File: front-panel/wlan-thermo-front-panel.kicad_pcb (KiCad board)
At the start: 2 copper layers, 54.7 x 43.5 mm, 26 parts, among them IC1 ME6211C33M5G-N, J1 PROG_HDR, J2 Conn_01x02, J3 Conn_01x02, Q1 UMH3N, SW1 SW_Push, SW2 RotaryEncoder_Switch, U1 ESP-12F, U2 SHT4x, U3 SSD1306

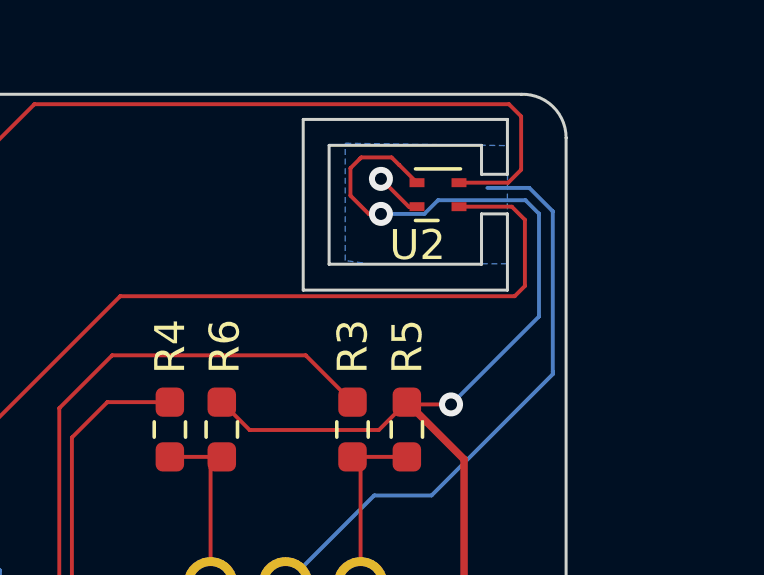
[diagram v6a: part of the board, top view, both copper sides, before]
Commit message: Removed (exposed) ground plane from sensor area (rev 1.2)
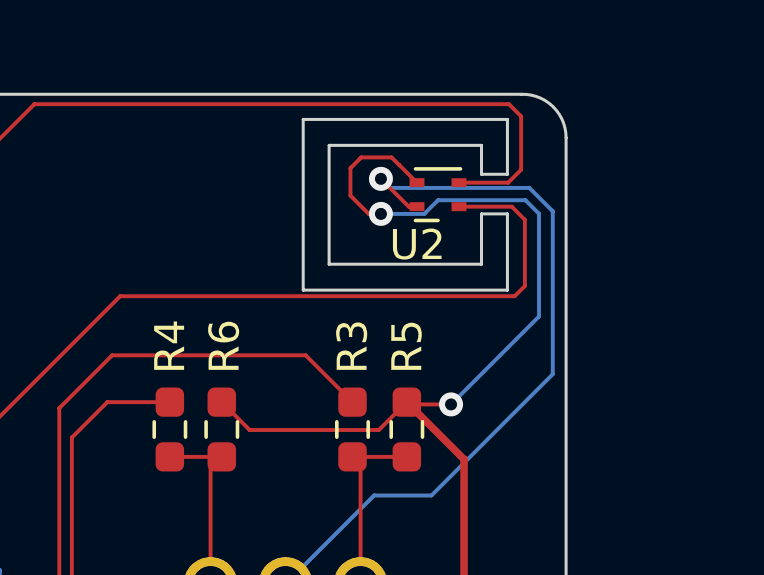
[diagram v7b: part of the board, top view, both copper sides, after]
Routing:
- net GND: track 47.9 -> 51.6 mm
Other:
- board text added: "WLAN Thermostat Frontpanel v1.2 (2023)"
- board text removed: "WLAN Thermostat Frontpanel v1.1 (2023)"
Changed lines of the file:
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@@
       (stroke (width 0) (type solid)) (fill solid) (layer "B.SilkS"))
   )
-  (gr_rect (start 146.5658 40.8806) (end 149.145 42.0116)
-    (stroke (width 0.15) (type solid)) (fill solid) (layer "B.Mask"))
-  (gr_rect (start 146.5742 38.2016) (end 149.1258 39.534)
-    (stroke (width 0.15) (type solid)) (fill solid) (layer "B.Mask"))
   (gr_line locked (start 82.0655 58.4313) (end 163.5995 58.4313)
     (stroke (width 0.15) (type default)) (layer "Dwgs.User"))
@@
     (effects (font (size 1 1) (thickness 0.15)) (justify left bottom mirror))
   )
-  (gr_text "WLAN Thermostat Frontpanel\nv1.1 (2023)" (at 151.81 46.1) (layer "B.SilkS")
+  (gr_text "WLAN Thermostat Frontpanel\nv1.2 (2023)" (at 151.81 46.1) (layer "B.SilkS")
     (effects (font (size 1 1) (thickness 0.15)) (justify left bottom mirror))
   )
@@
   (via (at 103.68 68.8) (size 0.8) (drill 0.4) (layers "F.Cu" "B.Cu") (net 4))
   (via (at 110.12 62.96) (size 0.8) (drill 0.4) (layers "F.Cu" "B.Cu") (free) (net 4))
-  (segment (start 150.767802 39.57) (end 149.37 39.57) (width 0.13) (layer "B.Cu") (net 4))
-  (segment (start 151.55 45.68) (end 151.55 40.352198) (width 0.13) (layer "B.Cu") (net 4))
+  (segment (start 147.51 49.82) (end 151.55 45.78) (width 0.13) (layer "B.Cu") (net 4))
+  (segment (start 146.123001 39.57) (end 145.821401 39.2684) (width 0.13) (layer "B.Cu") (net 4))
+  (segment (start 151.55 45.78) (end 151.55 40.352198) (width 0.13) (layer "B.Cu") (net 4))
   (segment (start 142.642801 52.7755) (end 145.598301 49.82) (width 0.13) (layer "B.Cu") (net 4))
-  (segment (start 151.55 45.78) (end 151.55 45.68) (width 0.13) (layer "B.Cu") (net 4))
-  (segment (start 147.51 49.82) (end 151.55 45.78) (width 0.13) (layer "B.Cu") (net 4))
+  (segment (start 150.767802 39.57) (end 146.123001 39.57) (width 0.13) (layer "B.Cu") (net 4))
+  (segment (start 145.598301 49.82) (end 147.51 49.82) (width 0.13) (layer "B.Cu") (net 4))
   (segment (start 103.69 75.7204) (end 103.7004 75.71) (width 0.25) (layer "B.Cu") (net 4))
-  (segment (start 145.598301 49.82) (end 147.51 49.82) (width 0.13) (layer "B.Cu") (net 4))
+  (segment (start 151.55 40.352198) (end 150.767802 39.57) (width 0.13) (layer "B.Cu") (net 4))
   (segment (start 103.7004 75.71) (end 113.24 75.71) (width 0.25) (layer "B.Cu") (net 4))
-  (segment (start 151.55 40.352198) (end 150.767802 39.57) (width 0.13) (layer "B.Cu") (net 4))
   (segment (start 113.24 75.71) (end 114.88 74.07) (width 0.25) (layer "B.Cu") (net 4))
   (segment (start 146.431001 38.8028) (end 146.426401 38.8028) (width 0.13) (layer "F.Cu") (net 6))
@@
       )
     )
-  )
-  (zone (net 4) (net_name "GND") (layer "B.Cu") (hatch edge 0.5)
-    (priority 2)
-    (connect_pads yes (clearance 0.25))
-    (min_thickness 0.25) (filled_areas_thickness no)
-    (fill yes (thermal_gap 0) (thermal_bridge_width 0.5))
-    (polygon
-      (pts
-        (xy 144.632 38.0808)
-        (xy 150.0466 38.1608)
-        (xy 150.0212 42.0978)
-        (xy 145.542 42.1132)
-        (xy 144.632 41.9924)
-      )
-    )

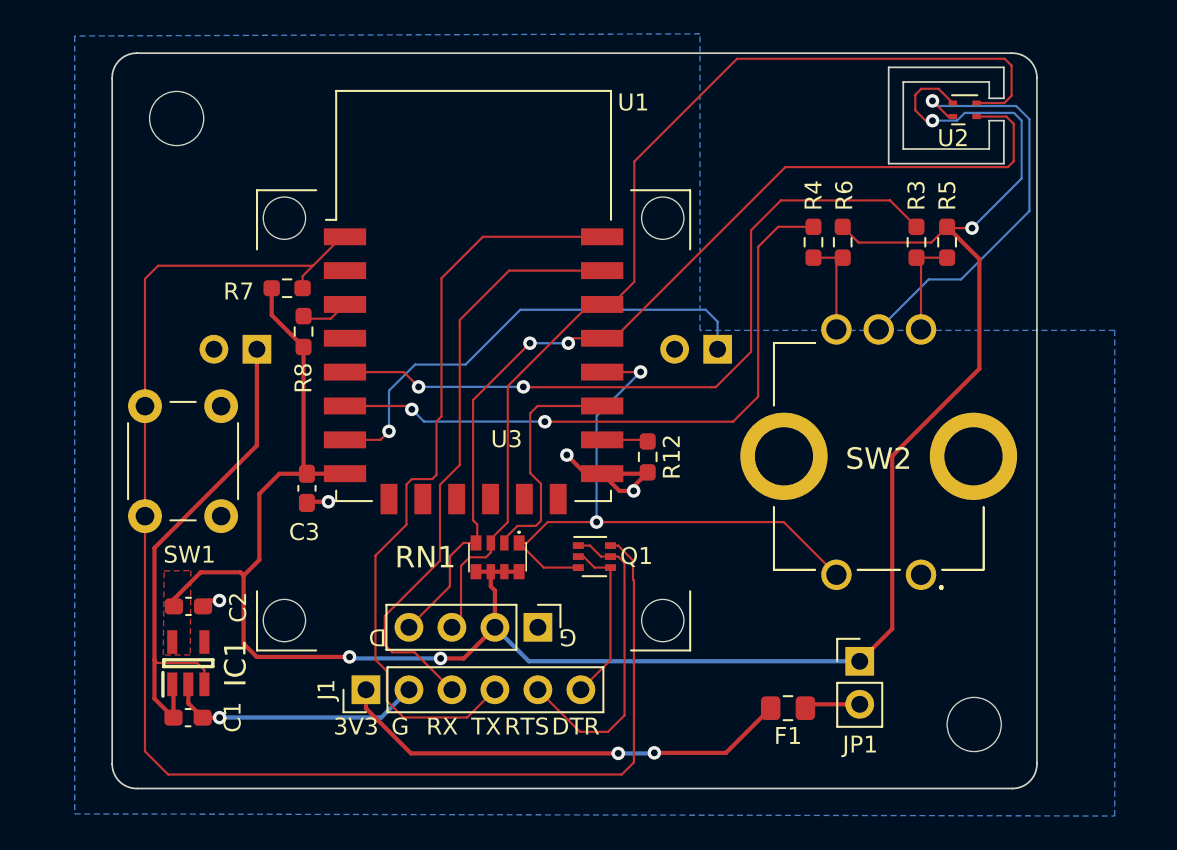
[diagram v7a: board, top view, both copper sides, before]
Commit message: Version 1.3b with side arm for temp sensor
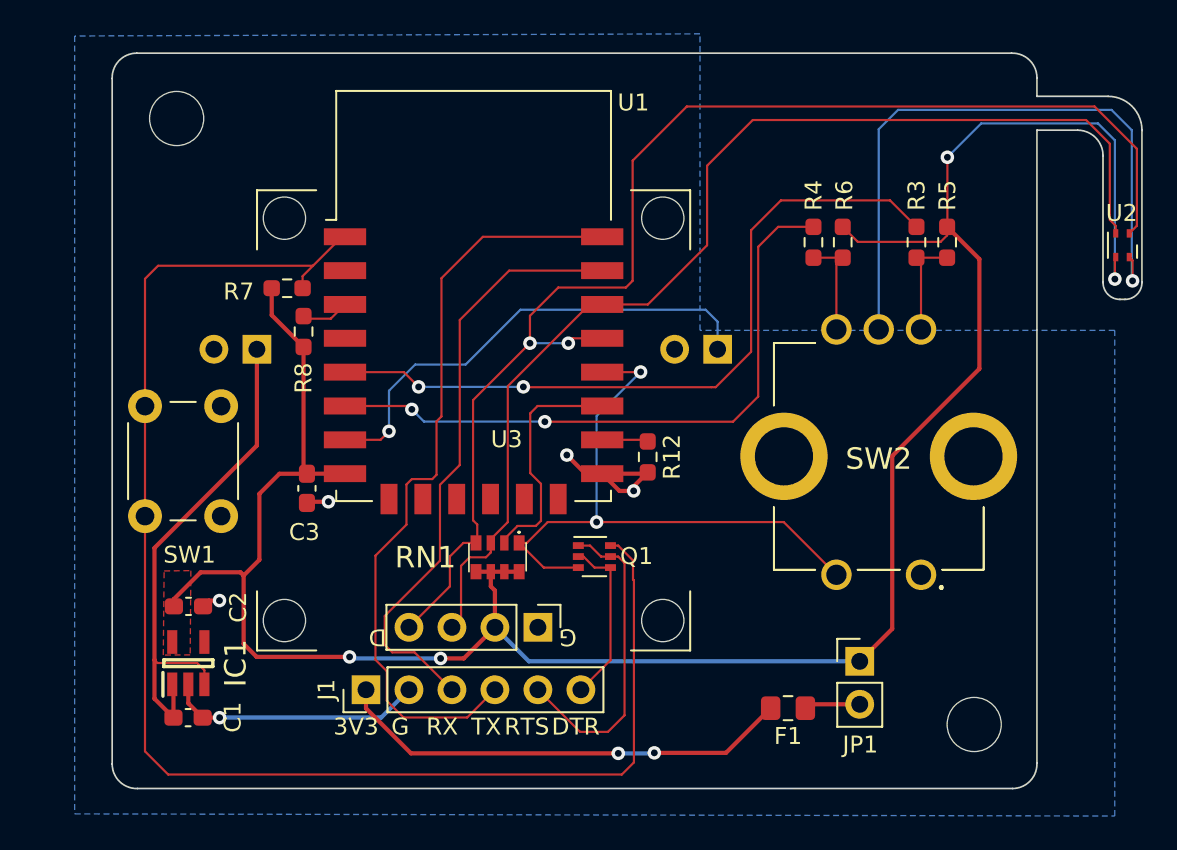
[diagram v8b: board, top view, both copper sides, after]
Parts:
- moved U2 12.3 mm to (157.1, 47.8), turned to -90 degrees
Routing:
- net GPIO4_SDA: track 58.1 -> 77.8 mm
- net GND: track 51.6 -> 64.8 mm
- net +3V3: track 131.8 -> 137.3 mm
- net GPIO5_SCL: track 62.3 -> 67.1 mm
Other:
- board size 54.7 x 43.5 mm -> 60.9 x 43.5 mm
- board text added: "WLAN Thermostat Frontpanel v1.3b (2023)"
- board text removed: "WLAN Thermostat Frontpanel v1.2 (2023)"
